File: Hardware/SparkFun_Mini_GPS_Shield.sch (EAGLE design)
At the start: 19 parts, among them J1 MICROSD_TINY, U1 GP735, U2 TXB0108, U3 AP2112K-3.3V

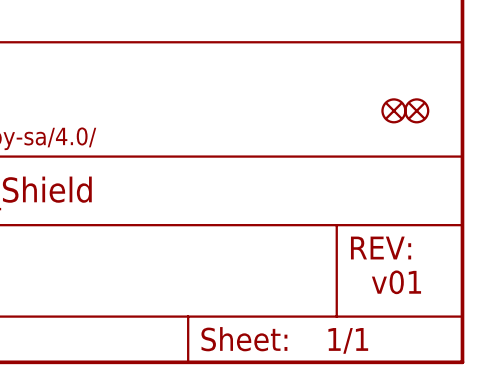
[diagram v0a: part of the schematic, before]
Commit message: V10 Changes
- Changed board name to "Mini GPS Shield".
- Extended board length to better support uSD card.
- Added v-score to board extention
- Changed control pin name to "CTL" instead of "CTR"
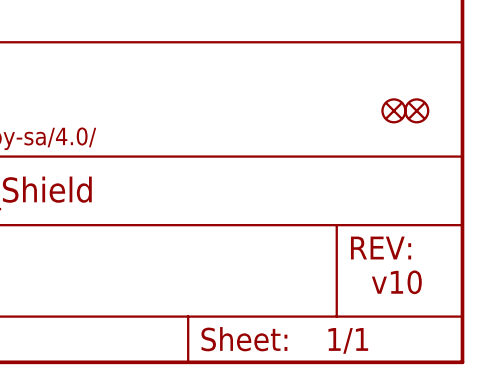
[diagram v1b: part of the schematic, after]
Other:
- note added: "v10"
- note removed: "v01"
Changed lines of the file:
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@@
 <wire x1="40.64" y1="53.34" x2="40.64" y2="0" width="0.1524" layer="97" style="shortdash"/>
 <text x="166.878" y="11.43" size="2.54" layer="94">Alex Wende</text>
-<text x="238.76" y="7.62" size="2.54" layer="94">v01</text>
+<text x="238.76" y="7.62" size="2.54" layer="94">v10</text>
 <text x="104.14" y="137.16" size="1.778" layer="97">V_BATT : 1.5V - 3.5V</text>
 </plain>

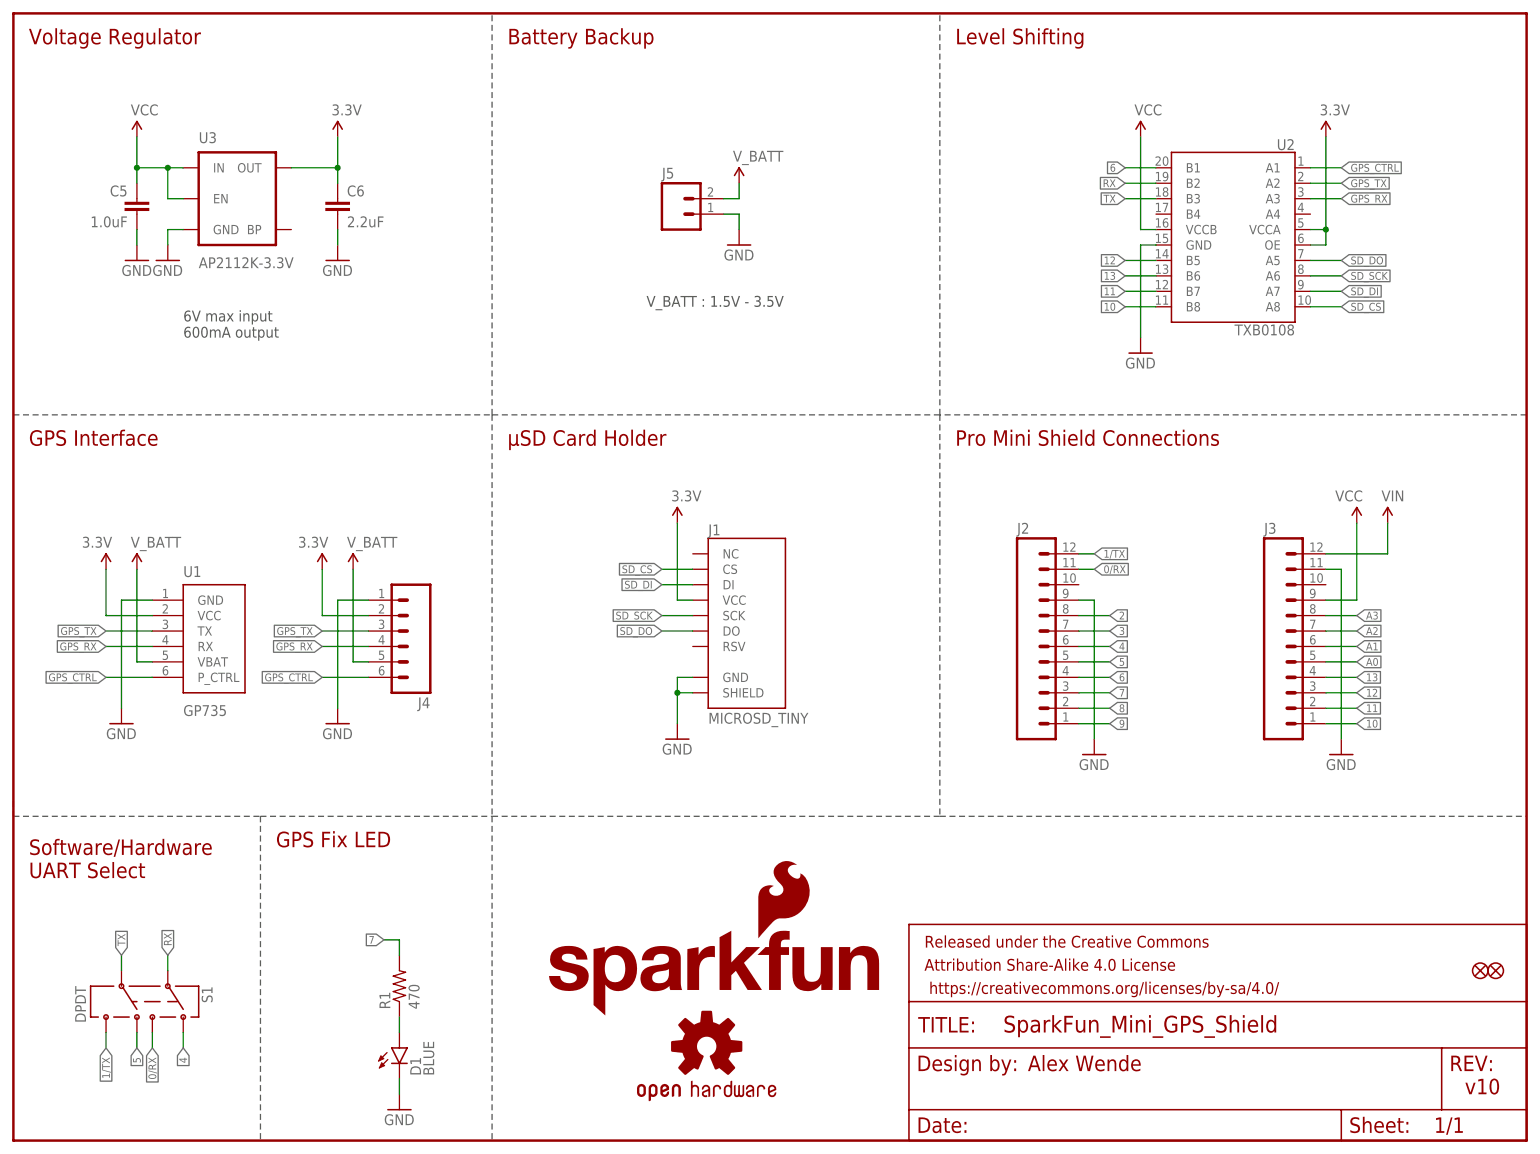
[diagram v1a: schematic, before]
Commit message: Changed UART net labels
0/RX and 1/TX are now RX/0 and TX/1
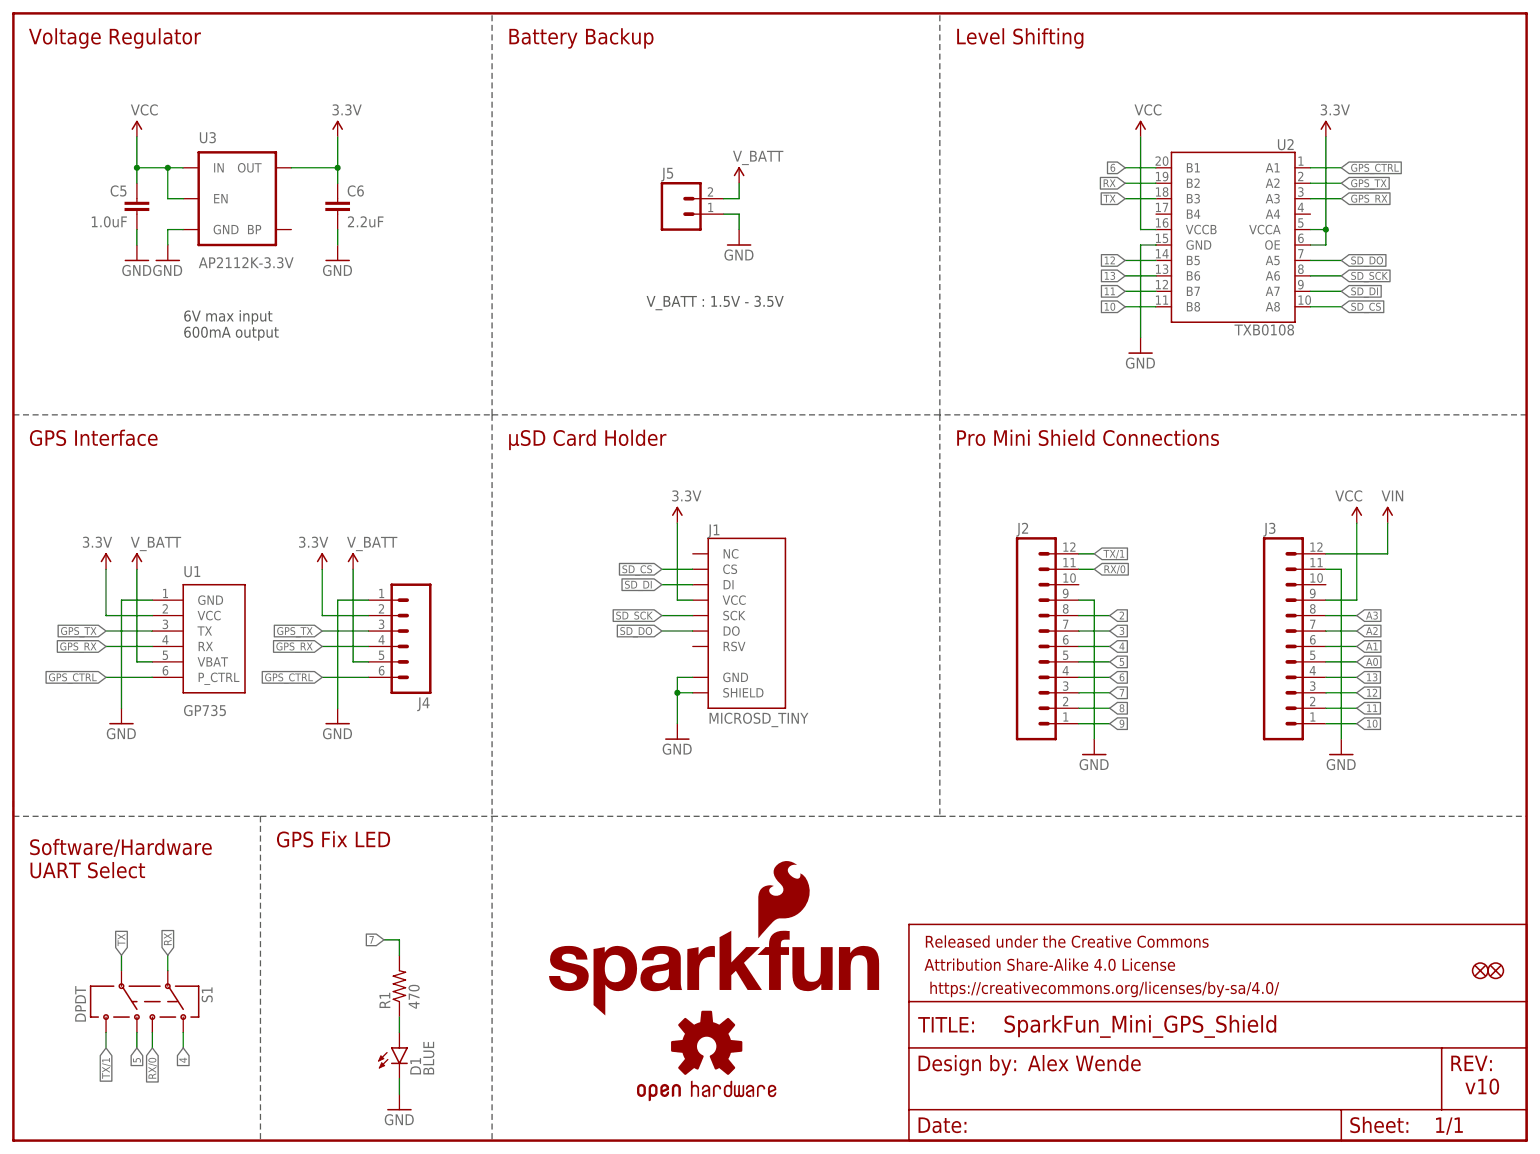
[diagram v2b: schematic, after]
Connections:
- net 0/RX renamed RX/0
- net 1/TX renamed TX/1
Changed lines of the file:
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@@
 </segment>
 </net>
-<net name="1/TX" class="0">
+<net name="TX/1" class="0">
 <segment>
 <pinref part="J2" gate="G$1" pin="12"/>
@@
 </segment>
 </net>
-<net name="0/RX" class="0">
+<net name="RX/0" class="0">
 <segment>
 <pinref part="J2" gate="G$1" pin="11"/>
